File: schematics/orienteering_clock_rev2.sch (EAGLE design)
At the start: 53 parts, among them IC1 TPIC6B595N, IC2 TPIC6B595N, J2 ICSP, Q1 IRFU9024V, Q2 IRFU9024V, Q3 IRFU9024V, Q4 IRFU9024V, Q5 IRFU9024V, Q6 IRFU9024V, T1 BC547, Y2 16MHz

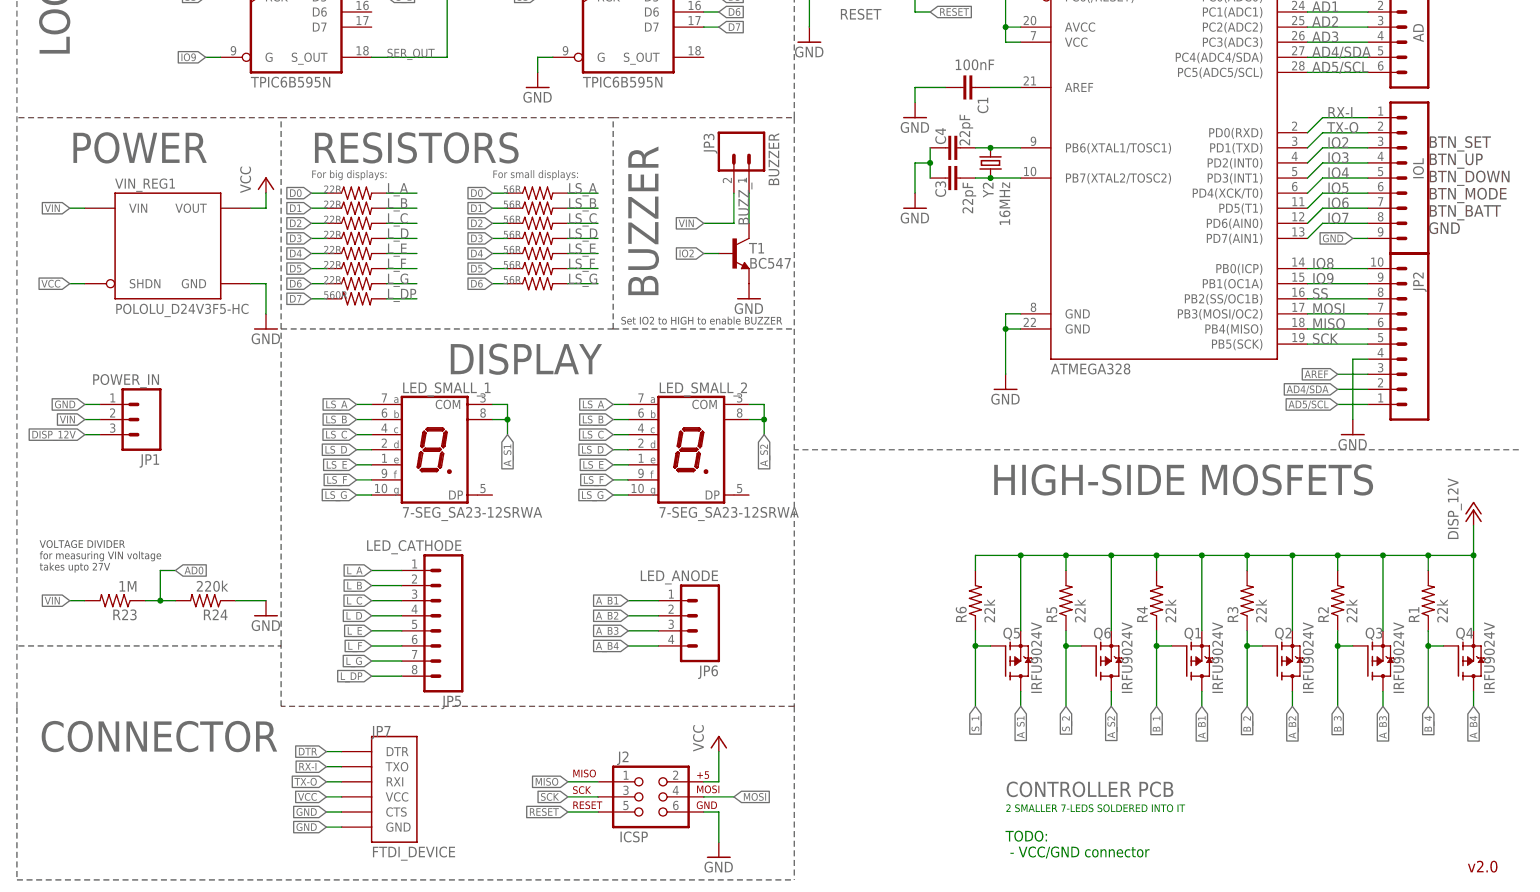
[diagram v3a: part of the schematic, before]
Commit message: schematics: improvements
- better packages for resistors
- slightly better placement
- added power_out outlet
- wider net for VCC
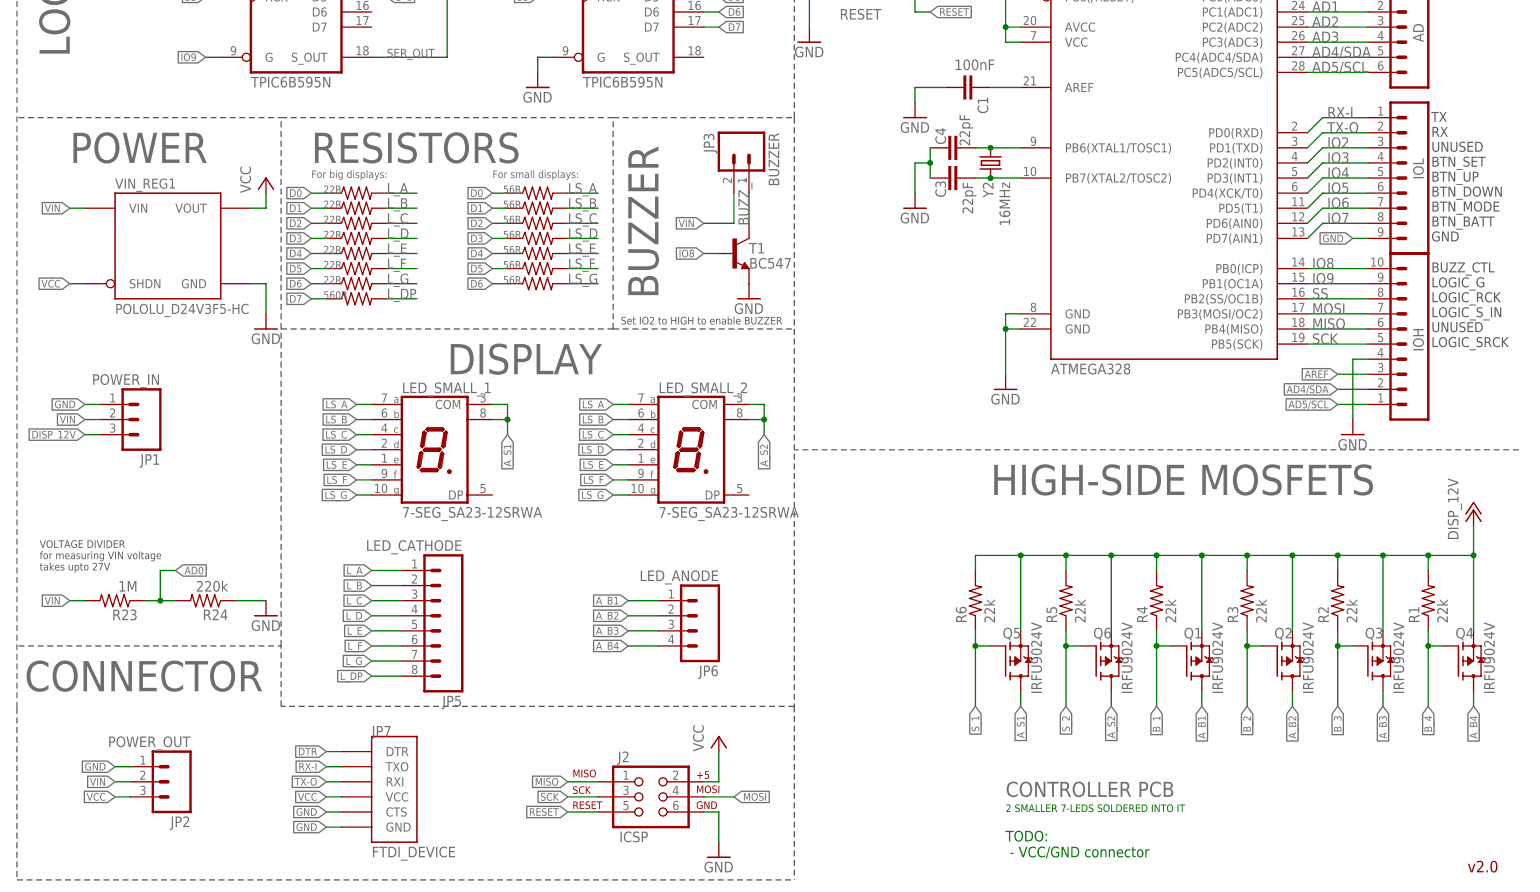
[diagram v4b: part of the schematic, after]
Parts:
- added IOH: M10LOCK, SparkFun-Connectors:M10LOCK
- JP2: value M10LOCK -> POWER_OUT; device SparkFun-Connectors:M10LOCK -> SparkFun-Connectors:M03POLAR
- R1, R2, R3, R4, R5, R6: device resistor:R-US_0204/5 -> resistor:R-US_0207/5V
- R10, R11, R12, R13, R21, R7, R8, R9: device resistor:R-US_0207/12 -> resistor:R-US_0207/10
- R23, R24: device resistor:R-US_0204/5 -> resistor:R-US_0207/10
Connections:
- net AD4/SDA: now also IOH.2; no longer JP2.2
- net AD5/SCL: now also IOH.1; no longer JP2.1
- net AREF: now also IOH.3; no longer JP2.3
- net GND: now also IOH.4, JP2.1; no longer JP2.4
- net IO2: no longer T1.B
- net IO8: now also IOH.10, T1.B; no longer JP2.10
- net IO9: now also IOH.9; no longer JP2.9
- net MISO: now also IOH.6; no longer JP2.6
- net MOSI: now also IOH.7; no longer JP2.7
- net SCK: now also IOH.5; no longer JP2.5
- net SS: now also IOH.8; no longer JP2.8
- net VCC: now also JP2.3
- net VIN: now also JP2.2
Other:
- note added: "BUZZ_CTL LOGIC_G LOGIC_RCK LOGIC_S_IN UNUSED LOGIC_SRCK"
- note added: "TX RX UNUSED BTN_SET BTN_UP BTN_DOWN BTN_MODE BTN_BATT GND"
- note removed: "BTN_SET BTN_UP BTN_DOWN BTN_MODE BTN_BATT GND"

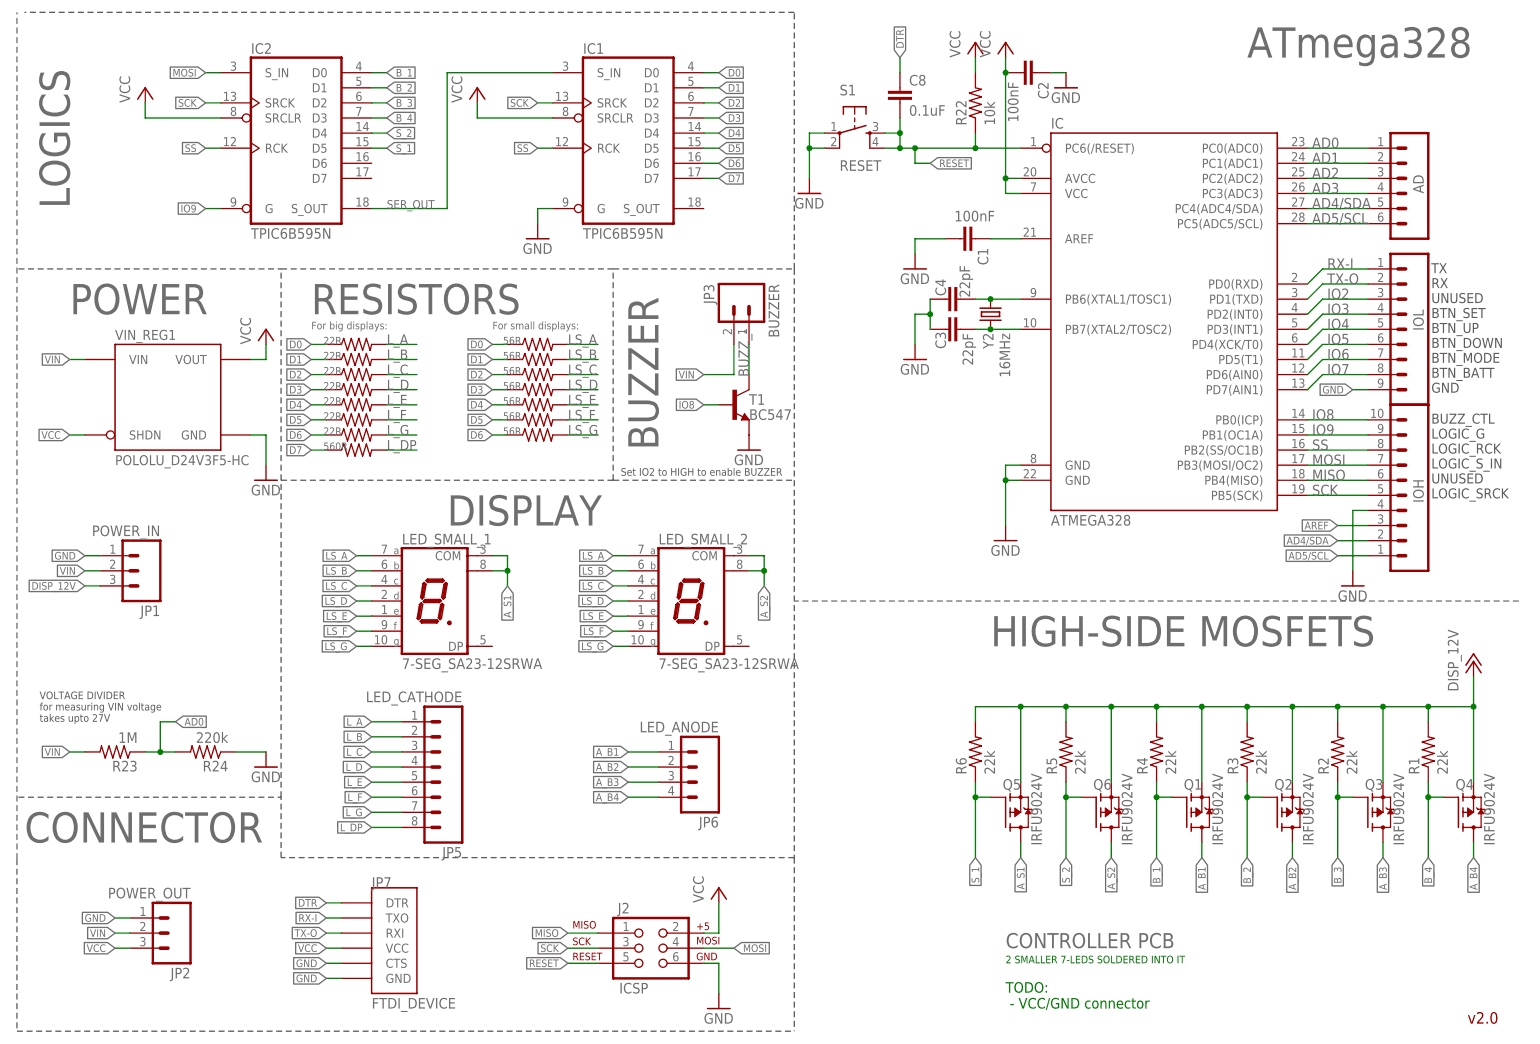
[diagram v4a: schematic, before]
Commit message: schematics: redid connections to comply with various DRC
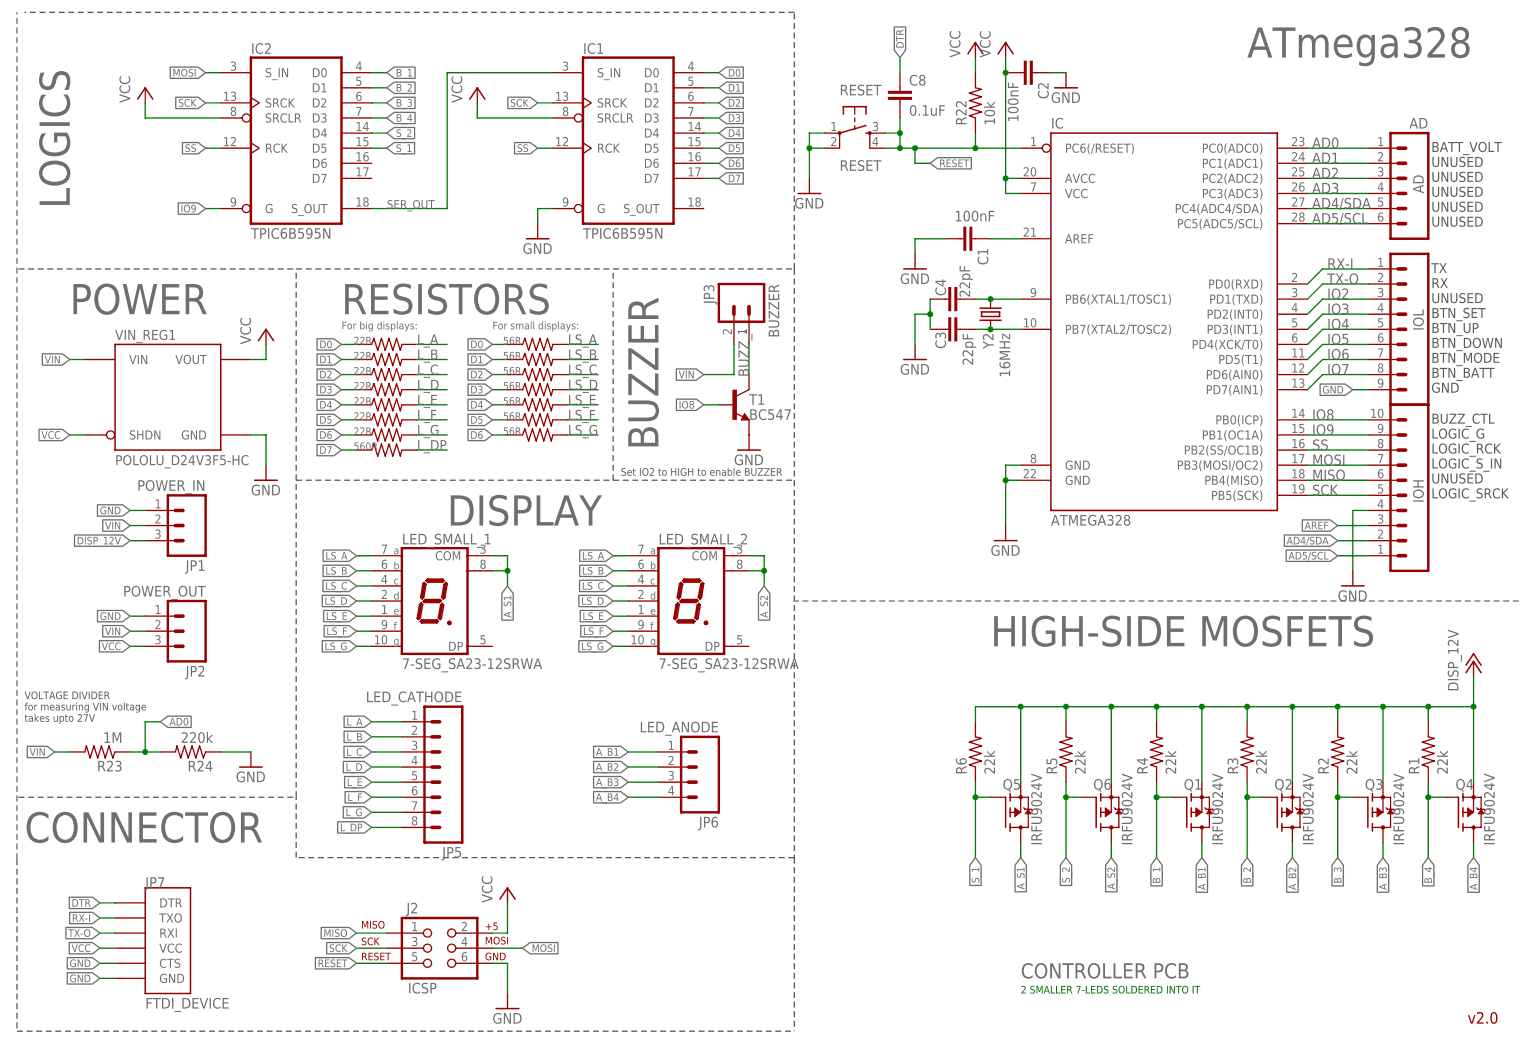
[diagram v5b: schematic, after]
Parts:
- AD: value (none) -> AD
- renumbered S1 to RESET
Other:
- note added: "BATT_VOLT UNUSED UNUSED UNUSED UNUSED UNUSED"
- note removed: "TODO: - VCC/GND connector"
- moved on the sheet: J2, JP1, JP2, JP7, R23, R24

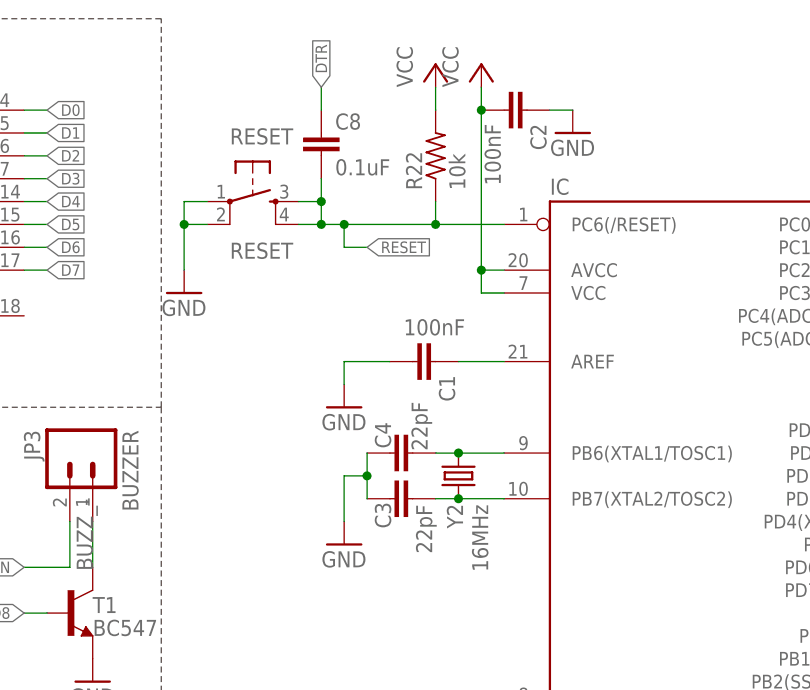
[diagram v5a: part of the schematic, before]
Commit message: schematics: part names smashing for silkscreen
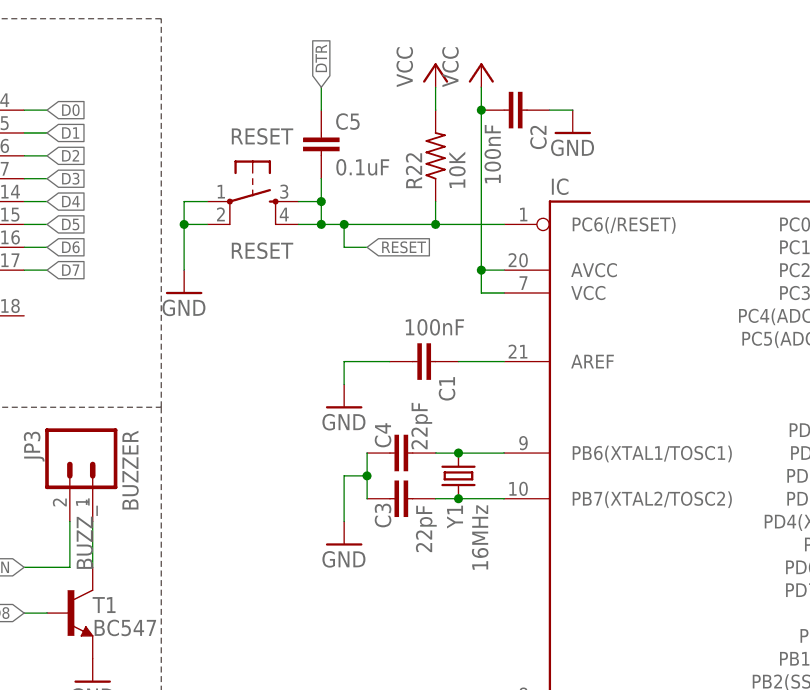
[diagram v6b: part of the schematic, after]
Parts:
- R22: value 10k -> 10K
- renumbered C8 to C5, Y2 to Y1
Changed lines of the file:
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@@
 <part name="GND3" library="SparkFun" deviceset="GND" device=""/>
 <part name="C1" library="SparkFun" deviceset="CAP" device="PTH" value="100nF"/>
-<part name="R22" library="resistor" deviceset="R-US_" device="0207/10" value="10k"/>
+<part name="R22" library="resistor" deviceset="R-US_" device="0207/10" value="10K"/>
 <part name="RESET" library="SparkFun" deviceset="TAC_SWITCH" device="PTH" value="RESET"/>
 <part name="GND5" library="SparkFun" deviceset="GND" device=""/>
@@
 <part name="GND7" library="SparkFun" deviceset="GND" device=""/>
 <part name="GND8" library="SparkFun" deviceset="GND" device=""/>
-<part name="C8" library="SparkFun" deviceset="CAP" device="PTH" value="0.1uF"/>
+<part name="C5" library="SparkFun" deviceset="CAP" device="PTH" value="0.1uF"/>
 <part name="IC" library="SparkFun-DigitalIC" deviceset="ATMEGA328P_PDIP" device="" value="ATMEGA328"/>
 <part name="IOH" library="SparkFun-Connectors" deviceset="M10" device="LOCK" value="M10LOCK"/>
 <part name="J2" library="SparkFun-Connectors" deviceset="AVR_SPI_PRG_6" device="2X3_LOCK" value="ICSP"/>
 <part name="GND26" library="SparkFun" deviceset="GND" device=""/>
-<part name="Y2" library="SparkFun-FreqCtrl" deviceset="CRYSTAL" device="HC49US" value="16MHz"/>
+<part name="Y1" library="SparkFun-FreqCtrl" deviceset="CRYSTAL" device="HC49US" value="16MHz"/>
 <part name="C3" library="SparkFun-Capacitors" deviceset="CAP" device="PTH" value="22pF"/>
 <part name="C4" library="SparkFun-Capacitors" deviceset="CAP" device="PTH" value="22pF"/>
@@
 <instance part="GND7" gate="1" x="129.54" y="114.3"/>
 <instance part="GND8" gate="1" x="119.38" y="38.1"/>
-<instance part="C8" gate="G$1" x="101.6" y="111.76"/>
+<instance part="C5" gate="G$1" x="101.6" y="111.76"/>
 <instance part="IC" gate="G$1" x="144.78" y="78.74"/>
 <instance part="IOH" gate="G$1" x="190.5" y="53.34" smashed="yes" rot="MR0">
@@
 <instance part="J2" gate="G$1" x="22.86" y="-30.48"/>
 <instance part="GND26" gate="1" x="177.8" y="30.48"/>
-<instance part="Y2" gate="G$1" x="116.84" y="76.2" smashed="yes" rot="R90">
+<instance part="Y1" gate="G$1" x="116.84" y="76.2" smashed="yes" rot="R90">
 <attribute name="NAME" x="117.348" y="70.358" size="1.778" layer="95" rot="R90"/>
 <attribute name="VALUE" x="120.142" y="65.532" size="1.778" layer="96" rot="R90"/>
@@
 <pinref part="RESET" gate="S" pin="4"/>
 <pinref part="IC" gate="G$1" pin="PC6(/RESET)"/>
-<pinref part="C8" gate="G$1" pin="2"/>
+<pinref part="C5" gate="G$1" pin="2"/>
 <wire x1="101.6" y1="109.22" x2="101.6" y2="106.68" width="0.1524" layer="91"/>
 <wire x1="104.14" y1="104.14" x2="104.14" y2="101.6" width="0.1524" layer="91"/>
@@
 <segment>
 <wire x1="101.6" y1="116.84" x2="101.6" y2="119.38" width="0.1524" layer="91"/>
-<pinref part="C8" gate="G$1" pin="1"/>
+<pinref part="C5" gate="G$1" pin="1"/>
 <label x="101.6" y="119.38" size="1.27" layer="95" rot="R90" xref="yes"/>
 </segment>
@@
 <pinref part="C4" gate="G$1" pin="2"/>
 <wire x1="121.92" y1="78.74" x2="116.84" y2="78.74" width="0.1524" layer="91"/>
-<pinref part="Y2" gate="G$1" pin="2"/>
+<pinref part="Y1" gate="G$1" pin="2"/>
 <junction x="116.84" y="78.74"/>
 <wire x1="116.84" y1="78.74" x2="114.3" y2="78.74" width="0.1524" layer="91"/>
@@
 <pinref part="C3" gate="G$1" pin="2"/>
 <wire x1="121.92" y1="73.66" x2="116.84" y2="73.66" width="0.1524" layer="91"/>
-<pinref part="Y2" gate="G$1" pin="1"/>
+<pinref part="Y1" gate="G$1" pin="1"/>
 <junction x="116.84" y="73.66"/>
 <wire x1="116.84" y1="73.66" x2="114.3" y2="73.66" width="0.1524" layer="91"/>
